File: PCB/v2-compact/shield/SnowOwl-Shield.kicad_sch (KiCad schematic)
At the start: 0 parts

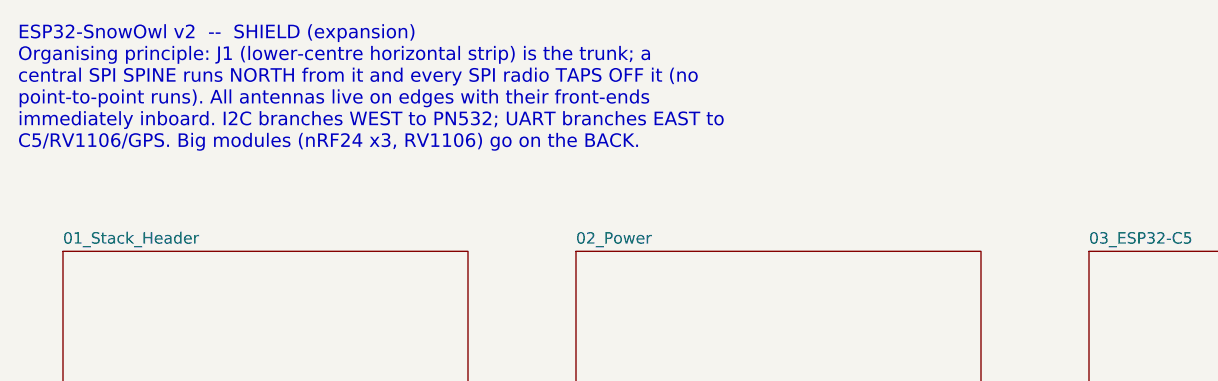
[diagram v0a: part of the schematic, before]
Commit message: PCB v2: grow to 70x100mm and adopt the C5-owns-radios architecture
Refit the outline to 70x100 after a footprint fit-check: 60x85 could not hold
the RV1106 SoM plus the C5 and nRF24 modules without cramming, which is what
forces congested traces.

- ESP32-C5 now masters the shield SPI spine; every SPI radio taps off it, so
  the whole radio fan-out stays on the shield next to the C5. The S3 commands
  the C5 over one UART on J1 and no SPI radio line crosses the stack header.
- Reflow both boards' zones for short-trace placement, sized to the real part
  footprints; keep the shared J1 datum (53.57, 106.0) so the boards still stack.
- Lock the J1 pinout: power + I2C(PN532) + S3<->C5 UART + S3<->RV1106 UART +
  IR + 1-Wire, with grounds spread for clean returns.
- Rewrite PLACEMENT.md as the updated contract; refresh the shield schematic
  intent note and both floorplan SVGs.
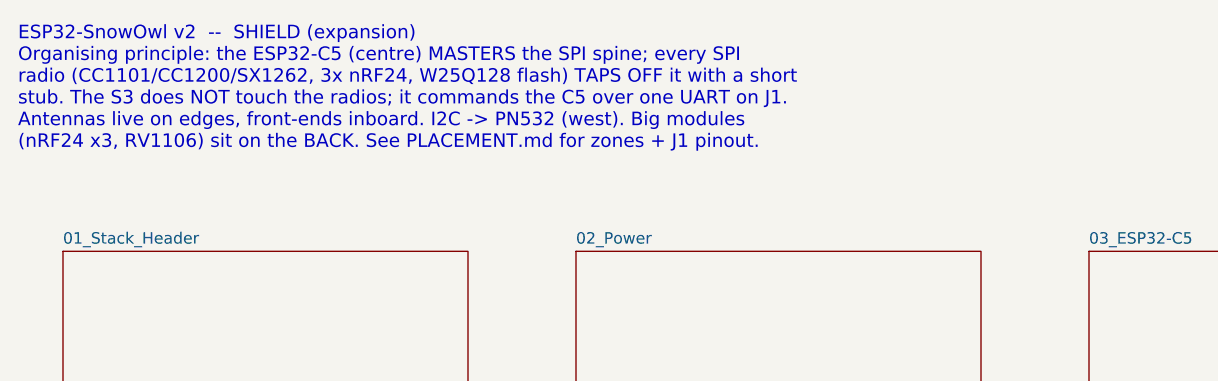
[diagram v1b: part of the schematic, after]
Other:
- note added: "ESP32-SnowOwl v2 -- SHIELD (expansion) Organising principle: the ESP32-C5 (centre) MASTERS the SPI spine; every SPI radio (CC1101/CC1200/SX1262, 3x nRF24, W25Q128 flash) TAPS OFF it with a short stub. The S3 does NOT touch the radios; it commands the C5 over one UART on J1. Antennas live on edges, front-ends inboard. I2C -> PN532 (west). Big modules (nRF24 x3, RV1106) sit on the BACK. See PLACEME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"
- note removed: "ESP32-SnowOwl v2 -- SHIELD (expansion) Organising principle: J1 (lower-centre horizontal strip) is the trunk; a central SPI SPINE runs NORTH from it and every SPI radio TAPS OFF it (no point-to-point runs). All antennas live on edges with their front-ends immediately inboard. I2C branches WEST to PN532; UART branches EAST to C5/RV1106/GPS. Big modules (nRF24 x3, RV1106) go on the BACK."
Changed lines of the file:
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@@
     (comment 1 "ESP32-SnowOwl v2 - compact 2-board stack"))
   (text "ESP32-SnowOwl v2  --  SHIELD (expansion)
-Organising principle: J1 (lower-centre horizontal strip) is the trunk; a
-central SPI SPINE runs NORTH from it and every SPI radio TAPS OFF it (no
-point-to-point runs). All antennas live on edges with their front-ends
-immediately inboard. I2C branches WEST to PN532; UART branches EAST to
-C5/RV1106/GPS. Big modules (nRF24 x3, RV1106) go on the BACK." (at 20 15 0)
+Organising principle: the ESP32-C5 (centre) MASTERS the SPI spine; every SPI
+radio (CC1101/CC1200/SX1262, 3x nRF24, W25Q128 flash) TAPS OFF it with a short
+stub. The S3 does NOT touch the radios; it commands the C5 over one UART on J1.
+Antennas live on edges, front-ends inboard. I2C -> PN532 (west). Big modules
+(nRF24 x3, RV1106) sit on the BACK. See PLACEMENT.md for zones + J1 pinout." (at 20 15 0)
     (effects (font (size 1.5 1.5)) (justify left top)))
   (sheet (at 25.0 40.0) (size 45.0 24.0) (fields_autoplaced)

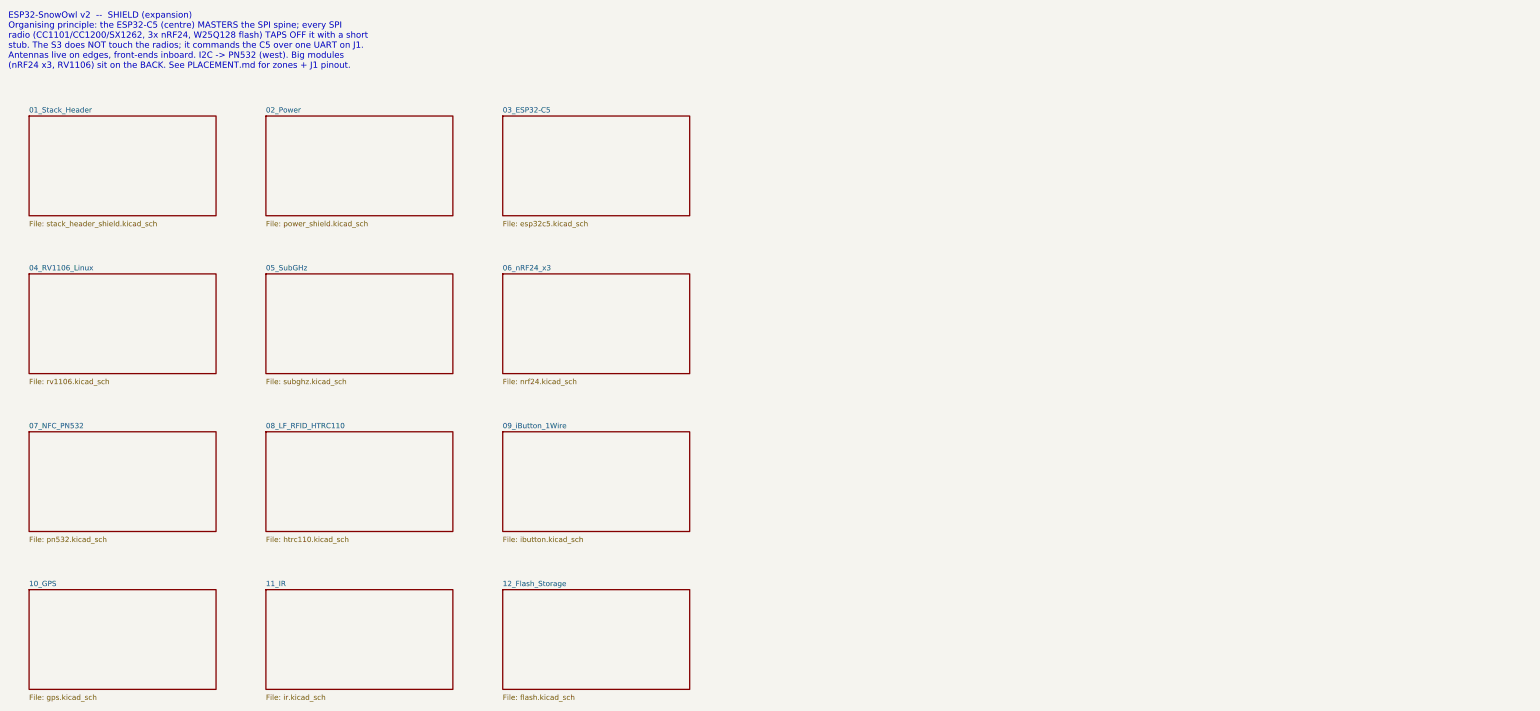
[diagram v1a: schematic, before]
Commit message: Schematics: fix hierarchy load, add verified generator, capture flash sheet
The v2 schematic roots were missing the per-sheet (instances) block, so the
projects would not load in KiCad (kicad-cli failed on both). Regenerate both
roots in a verified format (netlist export now succeeds on both boards).

Populate the first sub-sheet (12_Flash) as the proven pattern: real W25Q128
symbol, decoupling, wired to the SPI spine and power by global labels. Verified
by netlist (U12 pins map to FLASH_CS / SPI_SCK / SPI_MOSI / SPI_MISO / +3V3 / GND).
Remaining sub-sheets to follow the same pattern.
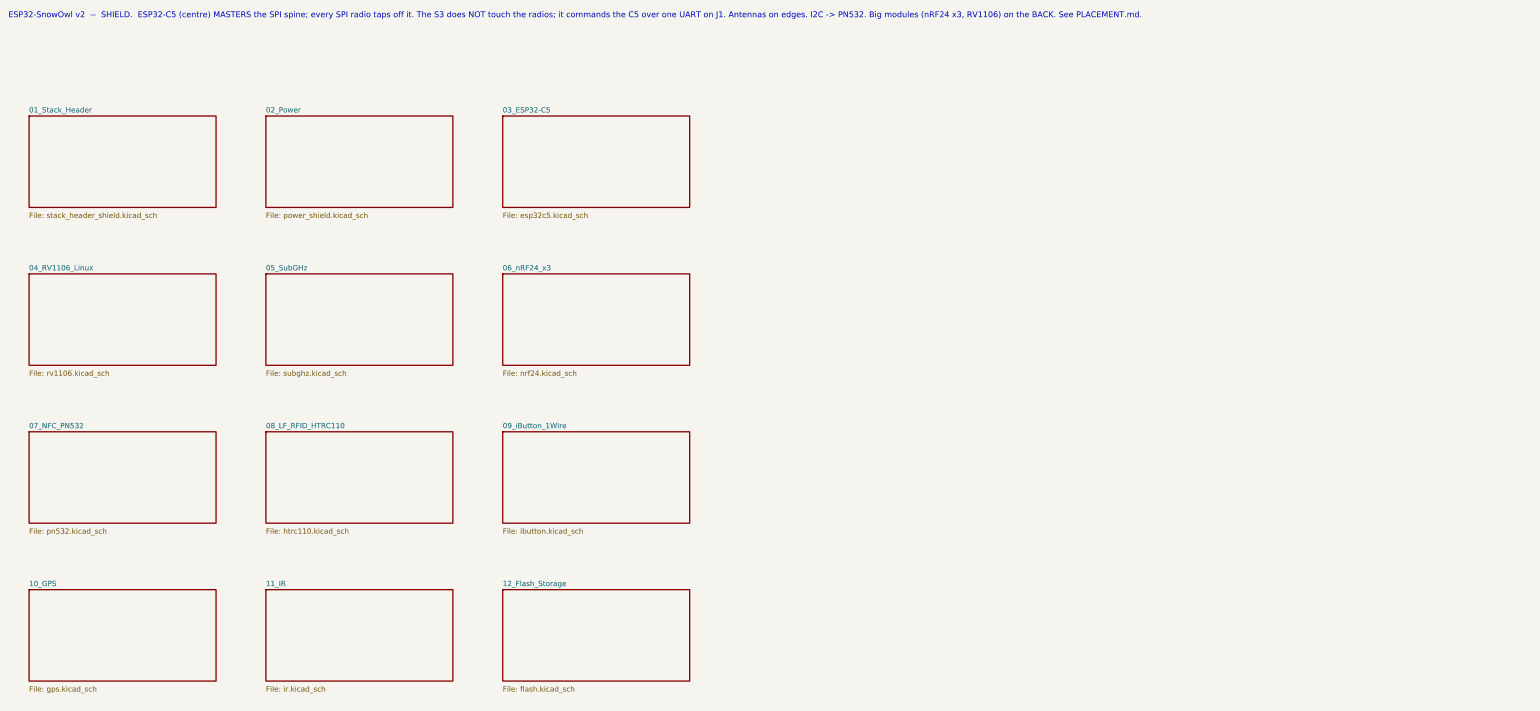
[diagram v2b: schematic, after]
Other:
- note added: "ESP32-SnowOwl v2 -- SHIELD. ESP32-C5 (centre) MASTERS the SPI spine; every SPI radio taps off it. The S3 does NOT touch the radios; it commands the C5 over one UART on J1. Antennas on edges. I2C -> PN532. Big modules (nRF24 x3, RV1106) on the BACK. See PLACEMENT.md."
- note removed: "ESP32-SnowOwl v2 -- SHIELD (expansion) Organising principle: the ESP32-C5 (centre) MASTERS the SPI spine; every SPI radio (CC1101/CC1200/SX1262, 3x nRF24, W25Q128 flash) TAPS OFF it with a short stub. The S3 does NOT touch the radios; it commands the C5 over one UART on J1. Antennas live on edges, front-ends inboard. I2C -> PN532 (west). Big modules (nRF24 x3, RV1106) sit on the BACK. See PLACEME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"
